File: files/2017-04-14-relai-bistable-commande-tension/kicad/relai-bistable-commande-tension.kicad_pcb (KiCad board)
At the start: 2 copper layers, 57.9 x 73.1 mm, 19 parts, among them T1 BC337, T2 BC337

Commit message: premier jet du pcb
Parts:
- moved T1 91.8 mm to (123.8, 128.9)
- moved D1 90.8 mm to (132.1, 137.8)
- moved D2 90.8 mm to (132.1, 134.0)
- moved T2 90.4 mm to (125.1, 123.2)
- moved J3 89.6 mm to (83.8, 175.9)
- moved R0 89.6 mm to (133.3, 122.6)
- moved RB1 89.6 mm to (133.3, 144.1)
- moved J1 89.6 mm to (113.7, 175.9)
- moved J2 89.6 mm to (96.5, 175.9)
- moved R5 89.6 mm to (80.6, 172.1)
- moved R6 89.6 mm to (89.5, 141.6)
- moved ALIM1 89.6 mm to (122.6, 168.3)
- moved APM1 89.6 mm to (120.7, 133.3)
- moved OC1 89.6 mm to (83.2, 158.1)
- moved C1 88.3 mm to (98.4, 119.4)
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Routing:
- net GND: track 135.3 -> 204.3 mm
- net +3V3: track 24.6 -> 88.6 mm
- net Net-(D1-Pad2): track 20.4 -> 48.2 mm
- net Net-(D2-Pad2): track 14.0 -> 27.9 mm
- net Net-(R3-Pad2): track 8.50 -> 20.8 mm
- net Net-(C1-Pad1): track 39.1 -> 48.6 mm
- net Net-(R1-Pad1): track 9.13 -> 18.5 mm
- net Net-(APM1-Pad12): track 0.00 -> 4.49 mm
- net Net-(APM1-Pad11): track 0.00 -> 4.45 mm
- net Net-(APM1-Pad5): track 5.10 -> 6.72 mm
- net Net-(D1-Pad1): track 15.5 -> 14.9 mm

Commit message: modif PCB Kicad
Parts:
- moved C1 21.2 mm to (81.9, 132.7), turned to 90 degrees
- moved R2 19.8 mm to (98.4, 135.9)
- moved R1 19.7 mm to (90.8, 131.4)
- moved R4 15.9 mm to (103.5, 133.3)
- moved T1 11.3 mm to (120.7, 139.7), turned to 90 degrees
- moved T2 9.94 mm to (120.7, 132.1), turned to 270 degrees
- moved R3 9.92 mm to (111.1, 130.2)
- moved R0 7.73 mm to (132.1, 130.2), turned to 180 degrees
- moved OC1 4.45 mm to (83.2, 153.7)
- moved APM1 4.45 mm to (116.2, 133.3)
- moved R5 3.81 mm to (80.6, 168.3)
- moved R6 3.17 mm to (89.5, 138.4)
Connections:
- RB1 pad 3: Net-(J2-Pad1) -> AC
- RB1 pad 5: AC -> Net-(J2-Pad1)
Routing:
- net GND: track 204.3 -> 82.9 mm
- net Net-(C1-Pad1): track 48.6 -> 17.7 mm
- net Net-(R1-Pad1): track 18.5 -> 32.8 mm
- net Net-(APM1-Pad11): track 4.45 -> 18.4 mm
- net +3V3: track 88.6 -> 74.7 mm
- net Net-(APM1-Pad5): track 6.72 -> 19.6 mm
- net AC: track 35.1 -> 23.5 mm
- net Net-(J2-Pad1): track 42.3 -> 51.4 mm
- net Net-(D2-Pad2): track 27.9 -> 20.7 mm
- net Net-(D1-Pad2): track 48.2 -> 41.6 mm
- net Net-(D1-Pad1): track 14.9 -> 20.4 mm
- net Net-(APM1-Pad12): track 4.49 -> 8.41 mm
- net Net-(J3-Pad1): track 5.13 -> 8.94 mm
- net Net-(R3-Pad2): track 20.8 -> 18.5 mm
- net Net-(J3-Pad2): track 18.6 -> 20.6 mm
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
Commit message: pcb kicad
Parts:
- moved D2 68.7 mm to (76.2, 174.0), turned to 0 degrees
- moved D1 64.6 mm to (76.2, 170.2), turned to 0 degrees
- moved R0 64.2 mm to (87.0, 175.9), turned to 90 degrees
- moved RB1 63.4 mm to (84.0, 184.0)
- moved R5 57.4 mm to (125.7, 203.8)
- moved C1 57.2 mm to (125.7, 169.5), turned to 180 degrees
- moved OC1 55.9 mm to (125.7, 189.9), turned to 90 degrees
- moved J3 52.1 mm to (120.0, 213.4)
- moved T2 48.3 mm to (90.2, 169.5), turned to 0 degrees
- moved R6 48.2 mm to (120.7, 175.3), turned to 0 degrees
- moved J1 46.7 mm to (85.7, 213.4)
- moved R1 46.7 mm to (116.8, 170.2), turned to 180 degrees
- moved T1 46.4 mm to (90.2, 174.6), turned to 0 degrees
- moved APM1 45.6 mm to (92.1, 172.1), turned to 270 degrees
- moved R2 42.3 mm to (116.8, 174.0)
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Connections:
- J1 pad 1: Earth -> AC
- J1 pad 3: AC -> Earth
- J2 pad 1: Net-(J2-Pad1) -> Earth
- J2 pad 3: Earth -> Net-(J2-Pad3)
- OC1 pad 1: Net-(J3-Pad2) -> Net-(OC1-Pad1)
- OC1 pad 2: Net-(OC1-Pad2) -> Net-(J3-Pad2)
- R5 pad 2: Net-(OC1-Pad2) -> Net-(OC1-Pad1)
- RB1 pad 3: AC -> Net-(J2-Pad3)
- RB1 pad 5: Net-(J2-Pad1) -> AC
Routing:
- net Net-(J2-Pad3): track 0.00 -> 53.2 mm
- net Net-(J2-Pad1): track 51.4 -> 0.00 mm
- net +3V3: track 74.7 -> 51.7 mm
- net Net-(D1-Pad2): track 41.6 -> 22.6 mm
- net Net-(D2-Pad2): track 20.7 -> 29.7 mm
- net Net-(D1-Pad1): track 20.4 -> 27.7 mm
- net GND: track 82.9 -> 76.4 mm
- net AC: track 23.5 -> 18.0 mm
- net Net-(J3-Pad1): track 8.94 -> 13.4 mm
- net Net-(R3-Pad2): track 18.5 -> 22.6 mm
- net Net-(APM1-Pad5): track 19.6 -> 16.2 mm
- net Net-(OC1-Pad2): track 3.18 -> 0.00 mm
- net Net-(OC1-Pad1): track 0.00 -> 2.54 mm
- net Net-(ALIM1-Pad3): track 31.3 -> 33.2 mm
- net Net-(C1-Pad1): track 17.7 -> 19.2 mm
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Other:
- board size 57.9 x 73.1 mm -> 56 x 56 mm
- net class POWER removed

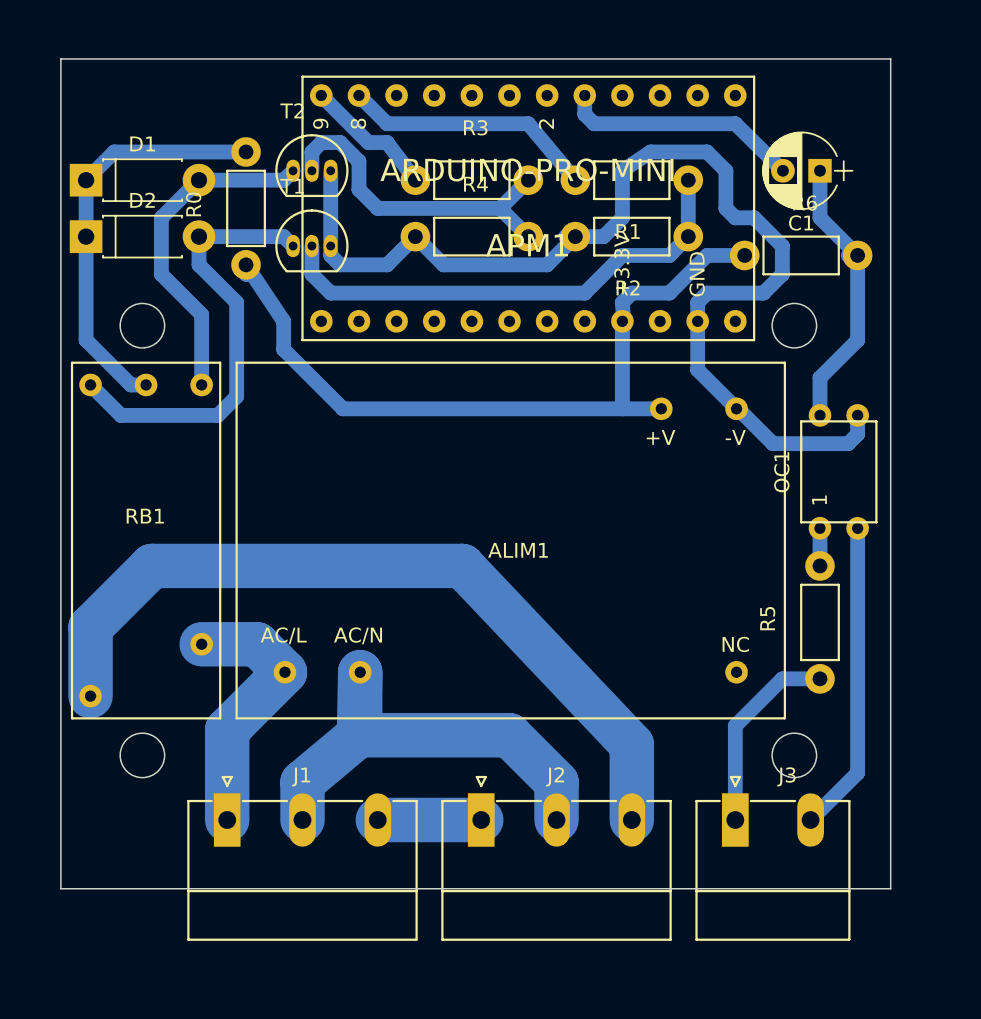
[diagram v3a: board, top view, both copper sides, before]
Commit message: plan de masse PCB
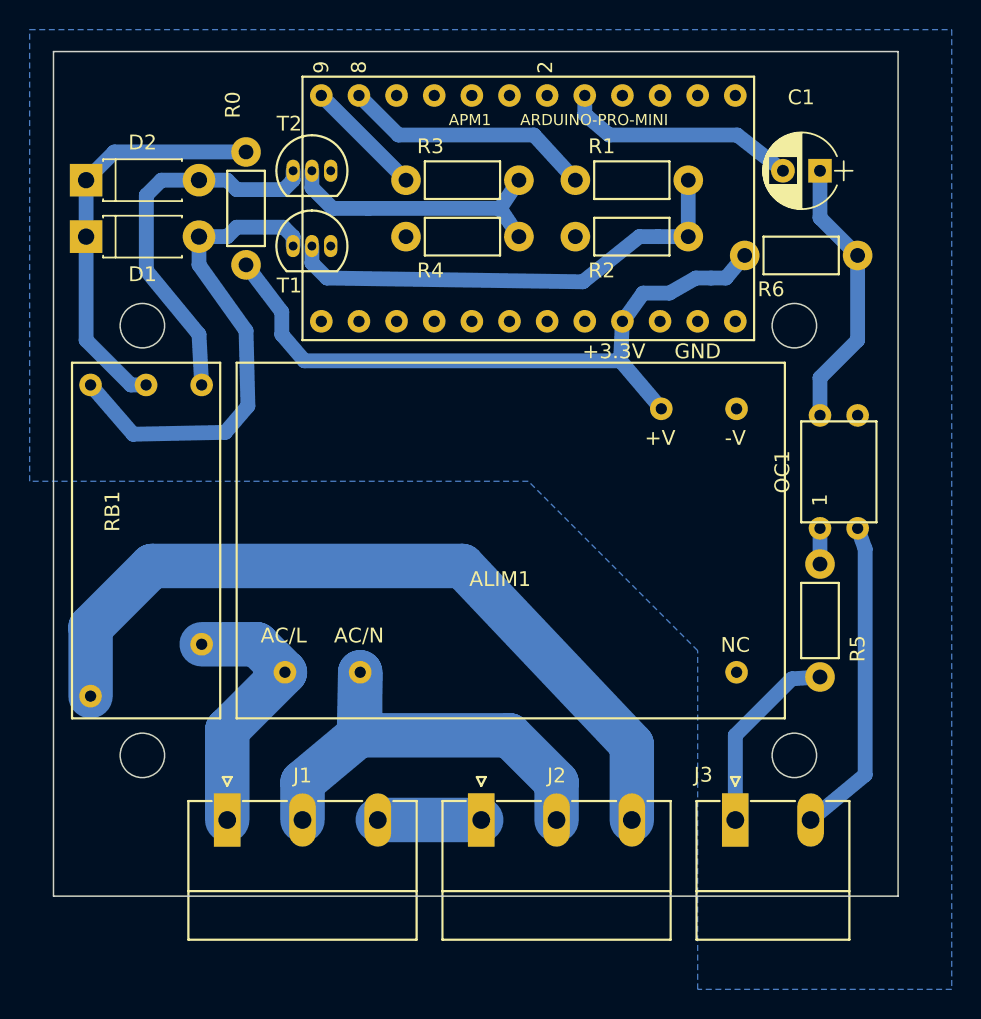
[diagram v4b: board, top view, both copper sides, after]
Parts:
- moved D1 3.81 mm to (76.2, 174.0)
- moved D2 3.81 mm to (76.2, 170.2)
- moved R3 0.63 mm to (97.8, 170.2)
- moved R4 0.63 mm to (97.8, 174.0)
- moved R5 0.13 mm to (125.7, 203.7)
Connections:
- RB1 pad -1: Net-(D2-Pad2) -> Net-(D1-Pad2)
- RB1 pad -6: Net-(D1-Pad2) -> Net-(D2-Pad2)
- T1 pad 1: Net-(D2-Pad2) -> Net-(D1-Pad2)
- T2 pad 1: Net-(D1-Pad2) -> Net-(D2-Pad2)
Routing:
- net GND: track 76.4 -> 0.00 mm
- net Net-(D1-Pad2): track 22.6 -> 32.9 mm
- net +3V3: track 51.7 -> 46.4 mm
- net Net-(D2-Pad2): track 29.7 -> 25.6 mm
- net Net-(R3-Pad2): track 22.6 -> 19.0 mm
- net Net-(R1-Pad1): track 33.2 -> 31.8 mm
- net Net-(APM1-Pad12): track 8.94 -> 8.08 mm
- net Net-(C1-Pad1): track 19.2 -> 18.6 mm
- net Net-(J3-Pad2): track 21.0 -> 21.5 mm
- added copper zone on B.Cu, net GND
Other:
- board size 56 x 56 mm -> 57 x 57 mm

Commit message: final
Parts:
- moved J1 0.63 mm to (85.7, 214.0)
- moved J2 0.63 mm to (102.9, 214.0)
- moved J3 0.63 mm to (120.0, 214.0)
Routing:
- net Net-(J3-Pad2): track 21.5 -> 0.00 mm
- net Net-(ALIM1-Pad3): track 33.2 -> 35.8 mm
- net Net-(J2-Pad3): track 53.2 -> 54.4 mm
- net AC: track 18.0 -> 19.3 mm
- added copper zone on B.Cu, net Net-(J3-Pad2)
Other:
- outline, holes or cut-outs redrawn
- board text added: "AC/DC IN1"
- board text added: "AC/DC IN2 (±60mA max)"
- board text added: "AC/L IN"
- board text added: "AC/L OUT"
- board text added: "AC/N IN"
- board text added: "AC/N OUT"
- board text added: "GND IN"
- board text added: "GND OUT"
- board text added: "OUILOGIQUE.COM"
- board text added: "OUILOGIQUE.COM Commande de relai bistable avril 2017"
